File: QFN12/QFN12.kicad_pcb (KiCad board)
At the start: 2 copper layers, 15.2 x 12.7 mm, 6 parts, among them J1 Conn_01x06, J2 Conn_02x06_Counter_Clockwise, J3 Conn_01x06, J5 Conn_01x03

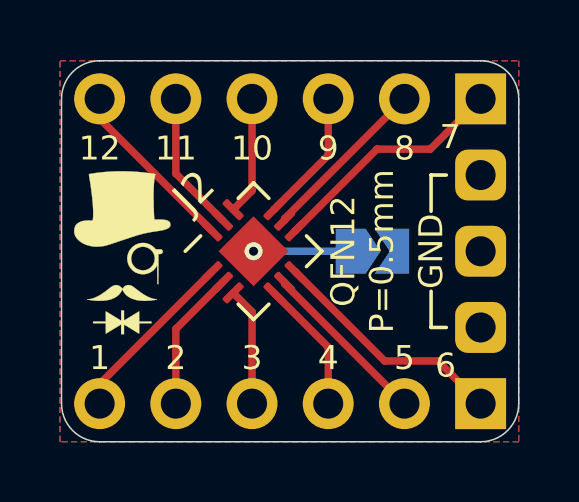
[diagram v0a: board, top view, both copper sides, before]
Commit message: Add 722AG footpring on QFN12 backside
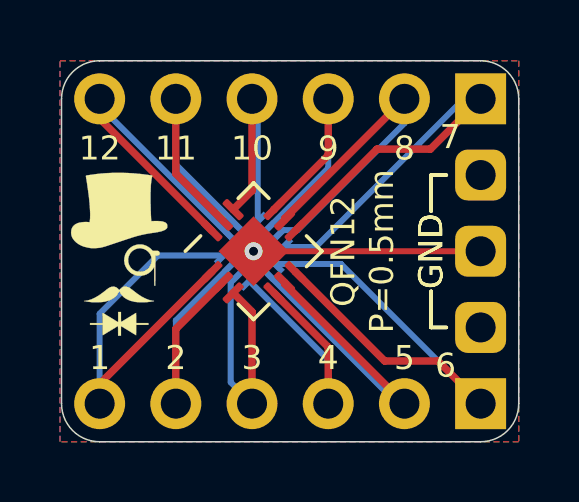
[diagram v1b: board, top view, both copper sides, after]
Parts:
- removed the G*** at (65.5, 42.0)
- removed JP1: SolderJumper_2_Open, Jumper:SolderJumper-2_P1.3mm_Open_TrianglePad1.0x1.5mm
- added G***: LOGO, logo:logo54x76, F.Cu at (65.4, 42.0)
- added G***: LOGO, logo:logo54x76, B.Cu at (65.4, 42.0)
- added J4: Conn_01x12, FUSB303TMX:QFN40P160X160X40-12N, B.Cu at (69.9, 41.9)
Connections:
- J1 pad 1: Net-(J2-Pad7) -> (no net)
- J1 pad 2: Net-(J2-Pad8) -> (no net)
- J1 pad 3: Net-(J2-Pad9) -> (no net)
- J1 pad 4: Net-(J2-Pad10) -> (no net)
- J1 pad 5: Net-(J2-Pad11) -> (no net)
- J1 pad 6: Net-(J2-Pad12) -> (no net)
- J2 pad 10: Net-(J2-Pad10) -> Net-(J1-Pad4)
- J2 pad 11: Net-(J2-Pad11) -> Net-(J1-Pad5)
- J2 pad 12: Net-(J2-Pad12) -> Net-(J1-Pad6)
- J2 pad 13: Net-(J2-Pad13) -> Net-(J5-Pad1)
- J2 pad 7: Net-(J2-Pad7) -> Net-(J1-Pad1)
- J2 pad 8: Net-(J2-Pad8) -> Net-(J1-Pad2)
- J2 pad 9: Net-(J2-Pad9) -> Net-(J1-Pad3)
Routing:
- net Net-(J1-Pad1): track 0.00 -> 17.1 mm
- net Net-(J1-Pad6): track 0.00 -> 13.1 mm
- net Net-(J1-Pad2): track 0.00 -> 12.4 mm
- net Net-(J1-Pad3): track 0.00 -> 10.4 mm
- net Net-(J1-Pad5): track 0.00 -> 9.96 mm
- net Net-(J2-Pad6): track 8.33 -> 17.1 mm
- net Net-(J2-Pad7): track 8.46 -> 0.00 mm
- net Net-(J1-Pad4): track 0.00 -> 8.12 mm
- net Net-(J3-Pad6): track 6.65 -> 14.6 mm
- net Net-(J5-Pad1): track 0.00 -> 7.57 mm, vias 0 -> 1
- net Net-(J2-Pad12): track 6.65 -> 0.00 mm
- net Net-(J2-Pad5): track 5.70 -> 12.1 mm
- net Net-(J2-Pad8): track 5.70 -> 0.00 mm
- net Net-(J2-Pad2): track 4.69 -> 10.1 mm
- net Net-(J2-Pad4): track 5.96 -> 11.1 mm
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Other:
- board text added: "QFN12 722AG"
